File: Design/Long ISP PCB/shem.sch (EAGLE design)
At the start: 41 parts, among them IC1 4511N, IC2 4511N, J1 9V_POWER_JACK, Q1 600mA/40V, Q2 600mA/40V, Q3 600mA/40V, Q4 600mA/40V, Q5 600mA/40V, U2 328P, U3 SN74HC595N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

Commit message: staged the files
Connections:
- net 9V: no longer IC1A.BI, IC1A.LT, IC1P.VDD, IC2A.BI, IC2A.LT, IC2P.VDD, PWR.P
- net VCC: now also IC1A.BI, IC1A.LT, IC1P.VDD, IC2A.BI, IC2A.LT, IC2P.VDD
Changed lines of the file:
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@@
 <part name="GND23" library="supply1" deviceset="GND" device=""/>
 <part name="GND24" library="supply1" deviceset="GND" device=""/>
-<part name="SUPPLY1" library="SparkFun-PowerSymbols" deviceset="12V" device="" value="9V"/>
-<part name="SUPPLY2" library="SparkFun-PowerSymbols" deviceset="12V" device="" value="9V"/>
-<part name="SUPPLY3" library="SparkFun-PowerSymbols" deviceset="12V" device="" value="9V"/>
-<part name="SUPPLY4" library="SparkFun-PowerSymbols" deviceset="12V" device="" value="9V"/>
-<part name="SUPPLY5" library="SparkFun-PowerSymbols" deviceset="12V" device="" value="9V"/>
 <part name="PWR" library="adafruit" deviceset="EG1218" device="S"/>
 <part name="D1" library="SparkFun-LED" deviceset="LED" device="3MM"/>
@@
 <part name="D7" library="SparkFun-LED" deviceset="LED" device="3MM"/>
 <part name="D8" library="SparkFun-LED" deviceset="LED" device="3MM"/>
+<part name="P+5" library="supply1" deviceset="VCC" device=""/>
+<part name="P+7" library="supply1" deviceset="VCC" device=""/>
+<part name="P+17" library="supply1" deviceset="VCC" device=""/>
+<part name="P+18" library="supply1" deviceset="VCC" device=""/>
 </parts>
 <sheets>
@@
 <instance part="IC2" gate="P" x="137.16" y="43.18"/>
 <instance part="GND24" gate="1" x="137.16" y="30.48"/>
-<instance part="SUPPLY1" gate="G$1" x="0" y="78.74" rot="R180"/>
-<instance part="SUPPLY2" gate="G$1" x="-33.02" y="53.34"/>
-<instance part="SUPPLY3" gate="G$1" x="-17.78" y="60.96"/>
-<instance part="SUPPLY4" gate="G$1" x="137.16" y="53.34"/>
-<instance part="SUPPLY5" gate="G$1" x="116.84" y="60.96"/>
 <instance part="PWR" gate="1" x="-2.54" y="88.9"/>
 <instance part="D1" gate="G$1" x="195.58" y="149.86" rot="R270"/>
@@
 <instance part="D7" gate="G$1" x="195.58" y="60.96" rot="R270"/>
 <instance part="D8" gate="G$1" x="195.58" y="45.72" rot="R270"/>
+<instance part="P+5" gate="VCC" x="-33.02" y="58.42"/>
+<instance part="P+7" gate="VCC" x="-17.78" y="60.96"/>
+<instance part="P+17" gate="VCC" x="116.84" y="60.96"/>
+<instance part="P+18" gate="VCC" x="137.16" y="55.88"/>
 </instances>
 <busses>
@@
 <pinref part="P+16" gate="VCC" pin="VCC"/>
 <wire x1="228.6" y1="43.18" x2="215.9" y2="43.18" width="0.1524" layer="91"/>
+</segment>
+<segment>
+<pinref part="IC1" gate="P" pin="VDD"/>
+<pinref part="P+5" gate="VCC" pin="VCC"/>
+<wire x1="-33.02" y1="55.88" x2="-33.02" y2="50.8" width="0.1524" layer="91"/>
+</segment>
+<segment>
+<pinref part="IC1" gate="A" pin="LT"/>
+<pinref part="P+7" gate="VCC" pin="VCC"/>
+<wire x1="-17.78" y1="58.42" x2="-17.78" y2="55.88" width="0.1524" layer="91"/>
+<pinref part="IC1" gate="A" pin="BI"/>
+<wire x1="-20.32" y1="55.88" x2="-20.32" y2="58.42" width="0.1524" layer="91"/>
+<wire x1="-20.32" y1="58.42" x2="-17.78" y2="58.42" width="0.1524" layer="91"/>
+<junction x="-17.78" y="58.42"/>
+</segment>
+<segment>
+<pinref part="IC2" gate="A" pin="LT"/>
+<pinref part="P+17" gate="VCC" pin="VCC"/>
+<wire x1="116.84" y1="58.42" x2="116.84" y2="55.88" width="0.1524" layer="91"/>
+<pinref part="IC2" gate="A" pin="BI"/>
+<wire x1="114.3" y1="55.88" x2="114.3" y2="58.42" width="0.1524" layer="91"/>
+<wire x1="114.3" y1="58.42" x2="116.84" y2="58.42" width="0.1524" layer="91"/>
+<junction x="116.84" y="58.42"/>
+</segment>
+<segment>
+<pinref part="IC2" gate="P" pin="VDD"/>
+<pinref part="P+18" gate="VCC" pin="VCC"/>
+<wire x1="137.16" y1="53.34" x2="137.16" y2="50.8" width="0.1524" layer="91"/>
 </segment>
 </net>
@@
 <junction x="7.62" y="96.52"/>
 </segment>
-<segment>
-<pinref part="IC1" gate="P" pin="VDD"/>
-<wire x1="-33.02" y1="53.34" x2="-33.02" y2="50.8" width="0.1524" layer="91"/>
-<pinref part="SUPPLY2" gate="G$1" pin="12V"/>
-</segment>
-<segment>
-<pinref part="IC1" gate="A" pin="LT"/>
-<wire x1="-17.78" y1="60.96" x2="-17.78" y2="55.88" width="0.1524" layer="91"/>
-<pinref part="IC1" gate="A" pin="BI"/>
-<wire x1="-20.32" y1="55.88" x2="-20.32" y2="60.96" width="0.1524" layer="91"/>
-<wire x1="-20.32" y1="60.96" x2="-17.78" y2="60.96" width="0.1524" layer="91"/>
-<pinref part="SUPPLY3" gate="G$1" pin="12V"/>
-<junction x="-17.78" y="60.96"/>
-</segment>
-<segment>
-<pinref part="IC2" gate="A" pin="LT"/>
-<wire x1="116.84" y1="60.96" x2="116.84" y2="55.88" width="0.1524" layer="91"/>
-<pinref part="IC2" gate="A" pin="BI"/>
-<wire x1="114.3" y1="55.88" x2="114.3" y2="60.96" width="0.1524" layer="91"/>
-<wire x1="114.3" y1="60.96" x2="116.84" y2="60.96" width="0.1524" layer="91"/>
-<pinref part="SUPPLY5" gate="G$1" pin="12V"/>
-<junction x="116.84" y="60.96"/>
-</segment>
-<segment>
-<pinref part="IC2" gate="P" pin="VDD"/>
-<wire x1="137.16" y1="53.34" x2="137.16" y2="50.8" width="0.1524" layer="91"/>
-<pinref part="SUPPLY4" gate="G$1" pin="12V"/>
-</segment>
-<segment>
-<pinref part="SUPPLY1" gate="G$1" pin="12V"/>
-<pinref part="PWR" gate="1" pin="P"/>
-<wire x1="0" y1="78.74" x2="0" y2="83.82" width="0.1524" layer="91"/>
-</segment>
-</net>
+</net>

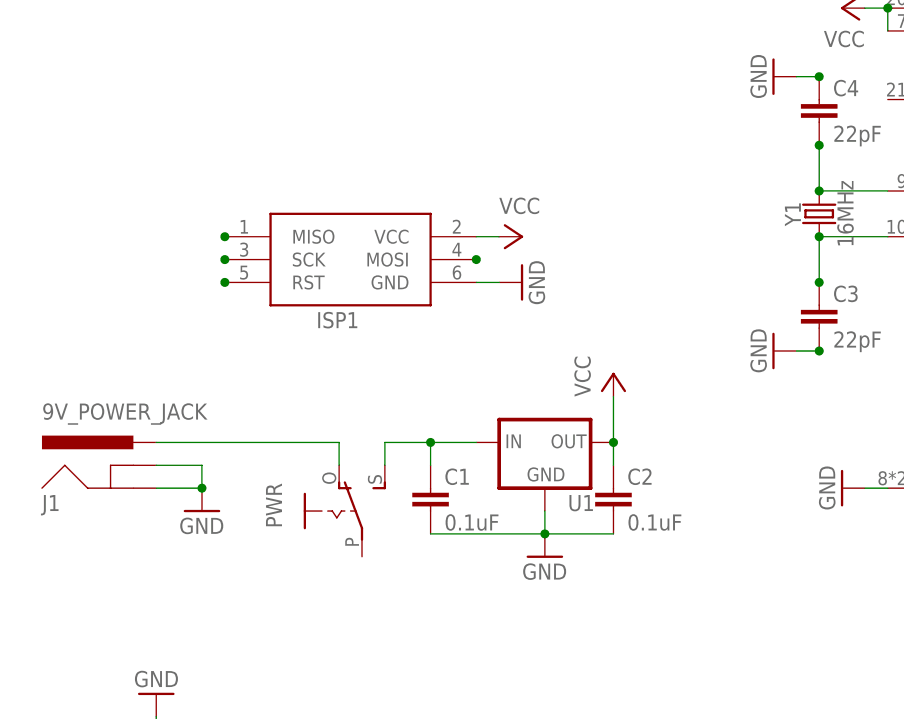
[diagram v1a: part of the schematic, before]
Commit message: added master power switch
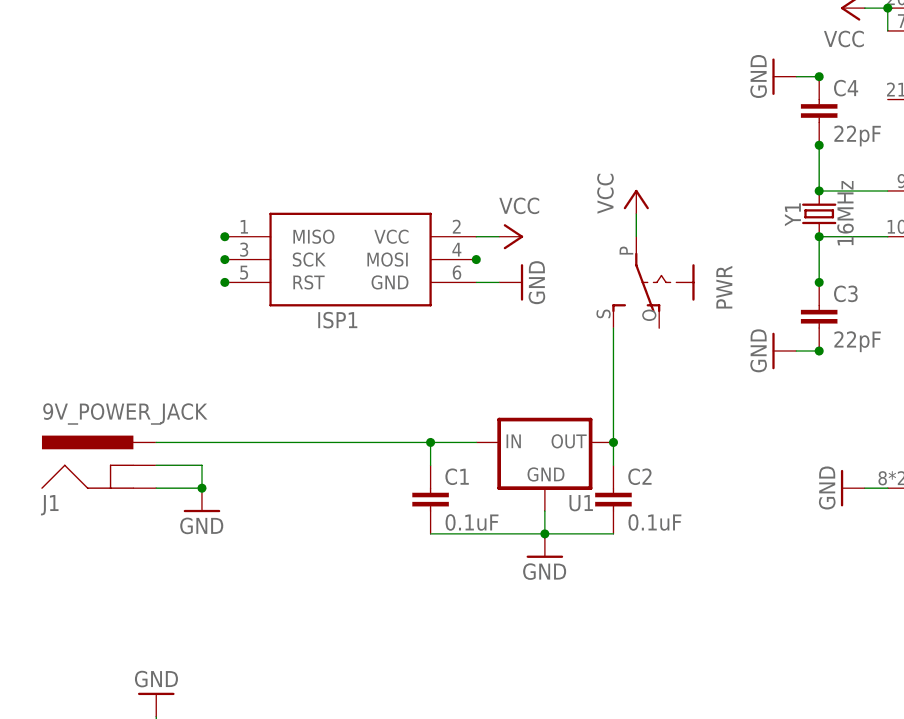
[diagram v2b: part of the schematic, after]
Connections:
- net 9V: now also J1.PWR; no longer PWR.S
- net N$1: now also C2.1, PWR.S, U1.OUT; no longer J1.PWR, PWR.O
- net VCC: now also PWR.P; no longer C2.1, U1.OUT
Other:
- moved on the sheet: PWR
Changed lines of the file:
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@@
 <part name="U2" library="SparkFun-IC-Microcontroller" deviceset="ATMEGA328P_PDIP" device="" value="328P"/>
 <part name="ISP1" library="adafruit" deviceset="AVRISP" device="-6"/>
-<part name="P+1" library="supply1" deviceset="VCC" device=""/>
 <part name="GND1" library="supply1" deviceset="GND" device=""/>
 <part name="GND2" library="supply1" deviceset="GND" device=""/>
@@
 <part name="GND23" library="supply1" deviceset="GND" device=""/>
 <part name="GND24" library="supply1" deviceset="GND" device=""/>
-<part name="PWR" library="adafruit" deviceset="EG1218" device="S"/>
 <part name="D1" library="SparkFun-LED" deviceset="LED" device="3MM"/>
 <part name="D2" library="SparkFun-LED" deviceset="LED" device="3MM"/>
@@
 <part name="P+17" library="supply1" deviceset="VCC" device=""/>
 <part name="P+18" library="supply1" deviceset="VCC" device=""/>
+<part name="PWR" library="adafruit" deviceset="EG1218" device="S"/>
+<part name="P+1" library="supply1" deviceset="VCC" device=""/>
 </parts>
 <sheets>
@@
 <instance part="U2" gate="U1" x="78.74" y="124.46"/>
 <instance part="ISP1" gate="G$1" x="-2.54" y="116.84"/>
-<instance part="P+1" gate="VCC" x="27.94" y="104.14"/>
 <instance part="GND1" gate="1" x="20.32" y="83.82"/>
 <instance part="GND2" gate="1" x="-17.78" y="88.9"/>
@@
 <instance part="IC2" gate="P" x="137.16" y="43.18"/>
 <instance part="GND24" gate="1" x="137.16" y="30.48"/>
-<instance part="PWR" gate="1" x="-2.54" y="88.9"/>
 <instance part="D1" gate="G$1" x="195.58" y="149.86" rot="R270"/>
 <instance part="D2" gate="G$1" x="195.58" y="134.62" rot="R270"/>
@@
 <instance part="P+17" gate="VCC" x="116.84" y="60.96"/>
 <instance part="P+18" gate="VCC" x="137.16" y="55.88"/>
+<instance part="PWR" gate="1" x="33.02" y="114.3" rot="R180"/>
+<instance part="P+1" gate="VCC" x="30.48" y="124.46"/>
 </instances>
 <busses>
@@
 <nets>
 <net name="VCC" class="0">
-<segment>
-<pinref part="U1" gate="G$1" pin="OUT"/>
-<pinref part="P+1" gate="VCC" pin="VCC"/>
-<wire x1="27.94" y1="101.6" x2="27.94" y2="96.52" width="0.1524" layer="91"/>
-<pinref part="C2" gate="G$1" pin="1"/>
-<wire x1="27.94" y1="96.52" x2="27.94" y2="93.98" width="0.1524" layer="91"/>
-<junction x="27.94" y="96.52"/>
-</segment>
 <segment>
 <pinref part="U2" gate="U1" pin="AVCC"/>
@@
 <pinref part="P+18" gate="VCC" pin="VCC"/>
 <wire x1="137.16" y1="53.34" x2="137.16" y2="50.8" width="0.1524" layer="91"/>
+</segment>
+<segment>
+<pinref part="PWR" gate="1" pin="P"/>
+<pinref part="P+1" gate="VCC" pin="VCC"/>
+<wire x1="30.48" y1="121.92" x2="30.48" y2="119.38" width="0.1524" layer="91"/>
 </segment>
 </net>
@@
 <wire x1="7.62" y1="96.52" x2="12.7" y2="96.52" width="0.1524" layer="91"/>
 <wire x1="7.62" y1="93.98" x2="7.62" y2="96.52" width="0.1524" layer="91"/>
+<pinref part="J1" gate="G$1" pin="PWR"/>
+<wire x1="-22.86" y1="96.52" x2="7.62" y2="96.52" width="0.1524" layer="91"/>
+<junction x="7.62" y="96.52"/>
+</segment>
+</net>
+<net name="N$1" class="0">
+<segment>
+<pinref part="U1" gate="G$1" pin="OUT"/>
+<pinref part="C2" gate="G$1" pin="1"/>
+<wire x1="27.94" y1="96.52" x2="27.94" y2="93.98" width="0.1524" layer="91"/>
 <pinref part="PWR" gate="1" pin="S"/>
-<wire x1="2.54" y1="93.98" x2="2.54" y2="96.52" width="0.1524" layer="91"/>
-<wire x1="2.54" y1="96.52" x2="7.62" y2="96.52" width="0.1524" layer="91"/>
-<junction x="7.62" y="96.52"/>
-</segment>
-</net>
-<net name="N$1" class="0">
-<segment>
-<pinref part="J1" gate="G$1" pin="PWR"/>
-<pinref part="PWR" gate="1" pin="O"/>
-<wire x1="-22.86" y1="96.52" x2="-2.54" y2="96.52" width="0.1524" layer="91"/>
-<wire x1="-2.54" y1="96.52" x2="-2.54" y2="93.98" width="0.1524" layer="91"/>
-</segment>
-</net>
+<wire x1="27.94" y1="96.52" x2="27.94" y2="109.22" width="0.1524" layer="91"/>
+<junction x="27.94" y="96.52"/>
+</segment>
+</net>
